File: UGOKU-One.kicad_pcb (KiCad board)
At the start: 2 copper layers, 70 x 70 mm, 57 parts, among them J2 SERVO, J3 Conn_02x03_Odd_Even, J4 14110413001000, J5 14110413001000, J6 14110413001000, P1 USB_C_Plug_USB2.0, Q2 SS8050, Q3 SS8050, SW1 PF1, SW4 SW_Push, SW5 SW_Push_DPDT, SW6 SW_Push, T4 PTS_1.5_2, T5 MultiBoardMini_Libraries:PTS_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, T6 PTS_1.5_2, U1 AMS1117-3.3, U2 CP2102N-A02-GQFN28, U3 TB67H450FNG_EL, U4 K7805M-1000R3, U5 ESP32-WROOM-32E, U8 TB67H450FNG_EL

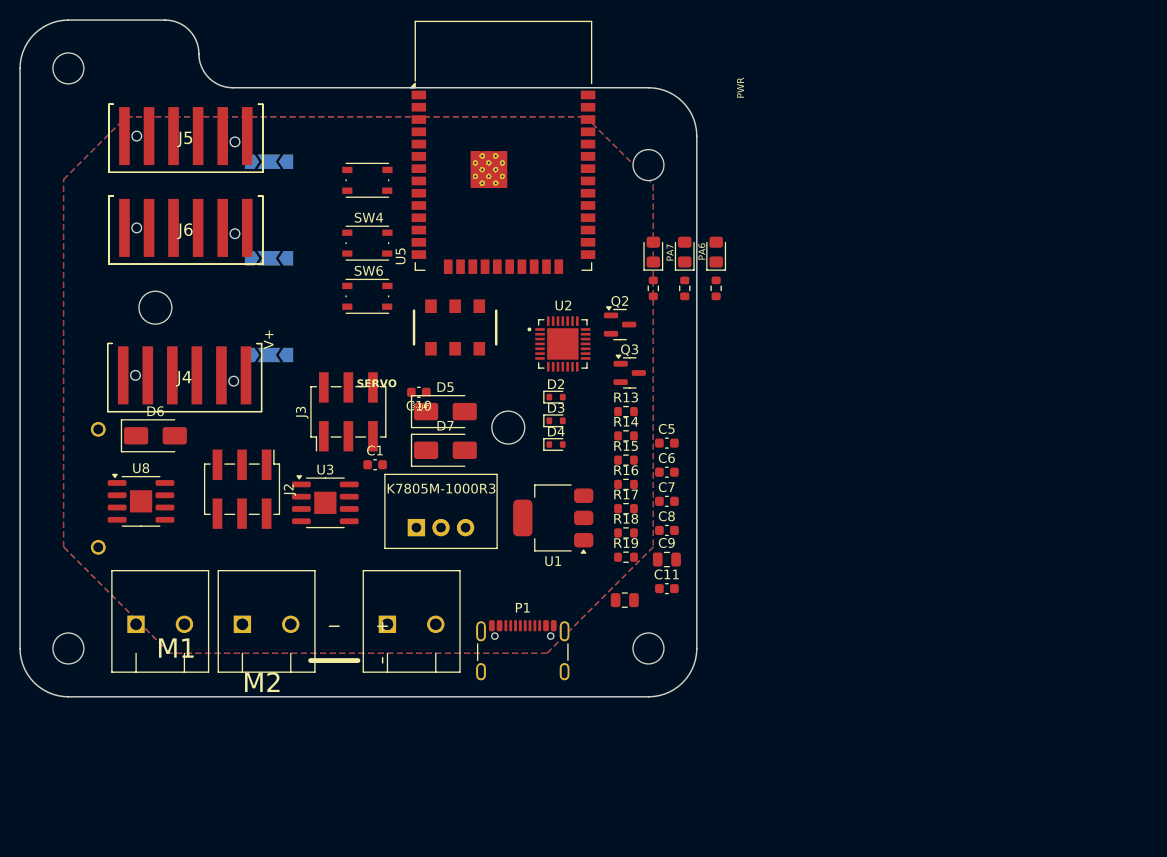
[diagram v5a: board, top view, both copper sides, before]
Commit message: Add IMU, FET
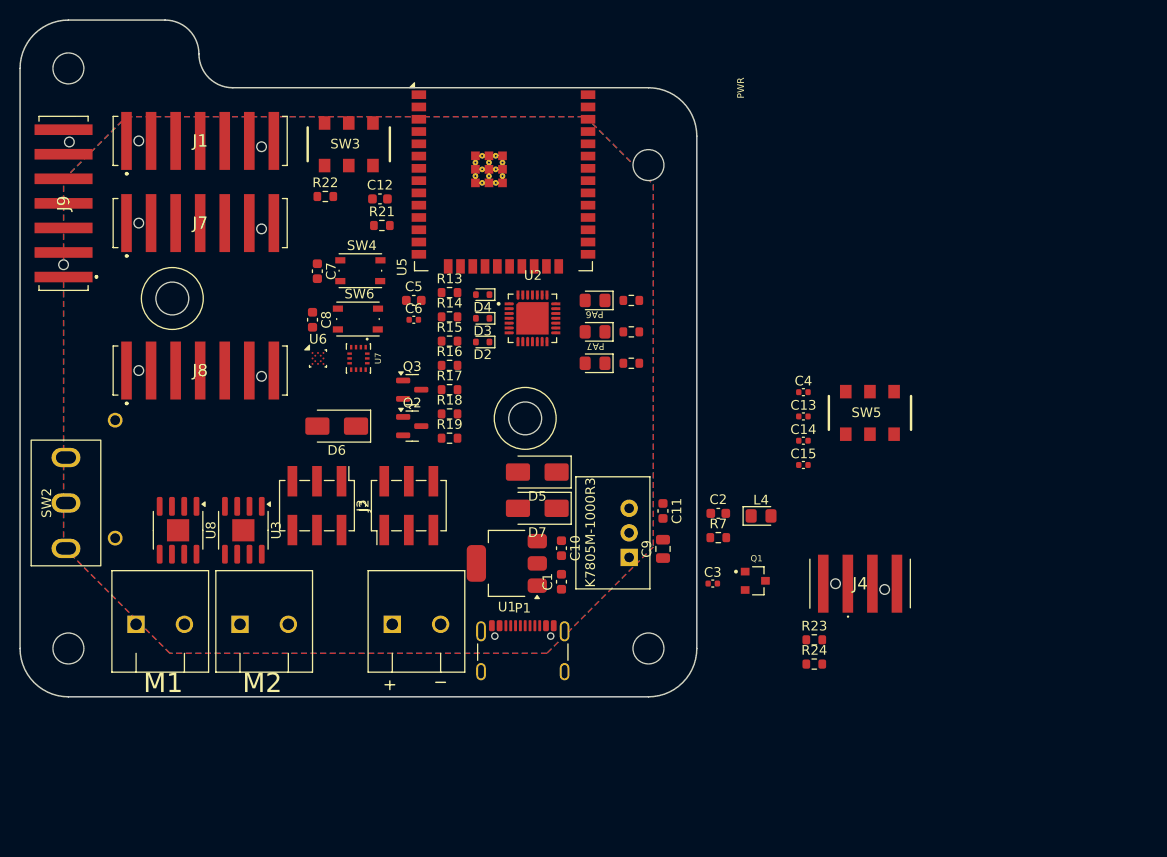
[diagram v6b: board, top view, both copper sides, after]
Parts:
- removed J5, J6: 14110413001000, 0_UGOKU-One_Lib:14110413001000
- removed JP1, JP2, JP3: Jumper_NC_Dual, Jumper:SolderJumper-3_P2.0mm_Open_TrianglePad1.0x1.5mm
- removed SW1: PF1, Button_Switch_SMD:SW_Push_1P1T_NO_Vertical_Wuerth_434133025816
- added C12: 0.1uF, Capacitor_SMD:C_0603_1608Metric, F.Cu at (2.23, -16.5)
- added C13: 0.1uF, Capacitor_SMD:C_0402_1005Metric, F.Cu at (46.0, 6.00)
- added C14: 0.1uF, Capacitor_SMD:C_0402_1005Metric, F.Cu at (46.0, 8.51)
- added C15: 0.1uF, Capacitor_SMD:C_0402_1005Metric, F.Cu at (46.0, 11.0)
- added C2: 22uF, Capacitor_SMD:C_0603_1608Metric, F.Cu at (37.2, 16.0)
- added C3: 0.1uF, Capacitor_SMD:C_0402_1005Metric, F.Cu at (36.6, 23.3)
- added J1: ENC/IO, 0_UGOKU-One_Lib:14110513001000, F.Cu at (-16.4, -22.5)
- added J7: ENC/IO, 0_UGOKU-One_Lib:14110513001000, F.Cu at (-16.4, -14.0)
- added J8: DAC, 0_UGOKU-One_Lib:14110513001000, F.Cu at (-16.4, 1.25)
- added J9: ADC, 0_UGOKU-One_Lib:14110513001000, F.Cu at (-30.5, -16.0)
- added L4: LED, LED_SMD:LED_0805_2012Metric_Pad1.15x1.40mm_HandSolder, F.Cu at (41.6, 16.3)
- added Q1: NMOS, 0_UGOKU-One_Lib:SOT-23F, F.Cu at (41.0, 23.0)
- added R21: 10k, Resistor_SMD:R_0603_1608Metric, F.Cu at (2.42, -13.8)
- added R22: 10k, Resistor_SMD:R_0603_1608Metric, F.Cu at (-3.42, -16.8)
- added R23: 10k, Resistor_SMD:R_0603_1608Metric, F.Cu at (47.1, 29.1)
- added R24: 100, Resistor_SMD:R_0603_1608Metric, F.Cu at (47.1, 31.6)
- added R7: 1k, Resistor_SMD:R_0603_1608Metric, F.Cu at (37.2, 18.5)
- added SW2: SW_SPDT, 0_UGOKU-One_Lib:SW_SS-12M11G5, F.Cu at (-30.2, 14.9)
- added SW3: SW_Slide_DPDT, 0_UGOKU-One_Lib:SSSS213202, F.Cu at (-1.00, -22.1)
- added U6: BMM150, Package_CSP:WLCSP-12_1.56x1.56mm_P0.4mm, F.Cu at (-4.18, 0.00)
- added U7: BMI270, 0_UGOKU-One_Lib:XDCR_BMI270, F.Cu at (0.00, 0.00)
- C4: value 0.1μF -> 0.1uF; footprint Capacitor_SMD:C_0805_2012Metric -> Capacitor_SMD:C_0402_1005Metric
- C6: footprint Capacitor_SMD:C_0603_1608Metric -> Capacitor_SMD:C_0402_1005Metric
- J4: value 14110413001000 -> 14110213001000; footprint 0_UGOKU-One_Lib:14110413001000 -> 0_UGOKU-One_Lib:14110213001000
- R13: value 10k -> 2K
- R14: value 10k -> 22.1k
- R15: value 10k -> 47.5k
- SW5: value SW_Push_DPDT -> SW_Slide_DPDT; footprint MultiBoardMini_Libraries:SSSS213202 -> 0_UGOKU-One_Lib:SSSS213202
- U2: footprint 0_UGOKU-One_Lib:QFN50P500X500X80-29N -> 0_UGOKU-One_Lib:IC_CP2102N-A02-GQFN28R
- U5: footprint RF_Module:ESP32-WROOM-32D -> RF_Module:ESP32-WROOM-32E
- moved J4 73.1 mm to (51.9, 23.3)
- moved SW5 43.8 mm to (52.9, 5.63)
- moved C7 43.3 mm to (-4.25, -9.03), turned to -90 degrees
- moved C8 42.6 mm to (-4.75, -4.00), turned to -90 degrees
- moved C6 30.6 mm to (5.72, -4.00)
- moved C5 30.1 mm to (5.72, -6.00)
- moved C4 28.4 mm to (46.0, 3.49), turned to 0 degrees
- moved Q2 23.9 mm to (5.56, 7.00)
- moved C1 22.8 mm to (21.0, 23.1), turned to 90 degrees
- moved Q3 22.6 mm to (5.56, 3.23)
- moved R13 22.0 mm to (9.43, -6.81)
- moved R14 22.0 mm to (9.43, -4.30)
- moved R15 22.0 mm to (9.43, -1.79)
- moved R16 22.0 mm to (9.43, 0.72)
- moved R17 22.0 mm to (9.43, 3.23)
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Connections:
- C10 pad 1: +3V3 -> 3V3
- C4 pad 1: PWR -> +3V3_IMU
- D6 pad 2: BAT_5V -> Net-(D6-A)
- J4 pad 1: Net-(J4-Pad1) -> MOT_PWR
- J4 pad 2: GND -> Net-(Q1-D)
- P1 pad A1: Net-(P1-GND-PadA1) -> GND
- P1 pad A12: Net-(P1-GND-PadA1) -> GND
- P1 pad B1: Net-(P1-GND-PadA1) -> GND
- P1 pad B12: Net-(P1-GND-PadA1) -> GND
- SW5 pad 2: Net-(SW5-B-Pad2) -> +3V3
- SW5 pad 3: GND -> +3V3_IMU
- SW5 pad 4: unconnected-(SW5-A-Pad4) -> +3V3_IMU
- SW5 pad 5: Net-(SW5-B-Pad2) -> +3V3
- SW5 pad 6: GND -> unconnected-(SW5-C-Pad6)
- U1 pad 3: +3V3 -> 3V3
- U5 pad 10: unconnected-(U5-IO25-Pad10) -> IO25
- U5 pad 11: unconnected-(U5-IO26-Pad11) -> IO26
- U5 pad 12: unconnected-(U5-IO27-Pad12) -> SERVO2
- U5 pad 14: MD2_IN1 -> unconnected-(U5-IO12-Pad14)
- U5 pad 16: MD2_IN2 -> MD1_IN2
- U5 pad 23: SERVO2 -> Slide_SW
- U5 pad 24: LED1 -> unconnected-(U5-IO2-Pad24)
- U5 pad 26: MD1_IN1 -> LED1
- U5 pad 27: unconnected-(U5-IO16-Pad27) -> LED3
- U5 pad 28: LED2 -> IO17
- U5 pad 29: MD1_IN2 -> MD1_IN1
- U5 pad 30: unconnected-(U5-IO18-Pad30) -> IO18
- U5 pad 31: unconnected-(U5-IO19-Pad31) -> IO19
- U5 pad 33: unconnected-(U5-IO21-Pad33) -> SDA
- U5 pad 36: unconnected-(U5-IO22-Pad36) -> SCL
- U5 pad 37: unconnected-(U5-IO23-Pad37) -> LED2
- U5 pad 4: unconnected-(U5-SENSOR_VP-Pad4) -> SENS_VP
- U5 pad 5: unconnected-(U5-SENSOR_VN-Pad5) -> SENS_VN
- U5 pad 6: unconnected-(U5-IO34-Pad6) -> IO34
- U5 pad 7: unconnected-(U5-IO35-Pad7) -> IO35
- U5 pad 8: unconnected-(U5-IO32-Pad8) -> MD2_IN1
- U5 pad 9: unconnected-(U5-IO33-Pad9) -> MD2_IN2
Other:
- board text removed: "3.3μF"
- board text removed: "3V3 5V"
- board text removed: "SERVO"
- board text removed: "V+"

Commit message: power layout draft
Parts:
- added C16: 10μF, Capacitor_SMD:C_0805_2012Metric, F.Cu at (-15.7, 19.8)
- added C17: 0.1μF, Capacitor_SMD:C_0402_1005Metric, F.Cu at (-13.9, 19.3)
- added C18: 0.1μF, Capacitor_SMD:C_0402_1005Metric, F.Cu at (-22.5, 19.7)
- added C19: 10μF, Capacitor_SMD:C_0805_2012Metric, F.Cu at (-23.7, 19.9)
- added D8: SS54, Diode_SMD:D_SMA, F.Cu at (15.0, 1.50)
- C12, C7, C8: footprint Capacitor_SMD:C_0603_1608Metric -> Capacitor_SMD:C_0402_1005Metric
- J4: footprint 0_UGOKU-One_Lib:14110213001000 -> 0_UGOKU-One_Lib:14010213102000
- R13, R14, R15, R16, R17, R18, R19, R21, R22, R23, R24: footprint Resistor_SMD:R_0603_1608Metric -> Resistor_SMD:R_0402_1005Metric
- moved C13 50.9 mm to (-4.25, -1.75)
- moved C4 50.3 mm to (-4.25, 1.75), turned to 180 degrees
- moved C15 49.3 mm to (-2.00, 0.00), turned to 90 degrees
- moved SW5 46.4 mm to (6.50, 4.30)
- moved C14 44.8 mm to (2.00, 0.00), turned to 90 degrees
- moved L4 35.4 mm to (13.8, -5.50), turned to 90 degrees
- moved C3 31.6 mm to (17.8, -2.08), turned to 90 degrees
- moved R24 31.3 mm to (22.0, 13.0), turned to 90 degrees
- moved R7 31.2 mm to (13.5, -1.75), turned to 90 degrees
- moved R23 31.1 mm to (20.5, 13.0), turned to 90 degrees
- moved J4 28.6 mm to (27.7, 8.00), turned to -90 degrees
- moved C2 27.7 mm to (16.2, -2.10), turned to 90 degrees
- moved Q3 27.2 mm to (27.8, -12.5), turned to 180 degrees
- moved Q2 26.4 mm to (28.2, -6.50)
- moved R4 24.0 mm to (4.35, -1.69), turned to 90 degrees
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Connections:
- net +3V3_IMU renamed 3V3_IMU
- net Net-(U3-OUT1) renamed /MD1_OUT1
- net Net-(U3-OUT2) renamed /MD1_OUT2
- net Net-(U8-OUT1) renamed /MD2_OUT1
- net Net-(U8-OUT2) renamed /MD2_OUT2
- C2 pad 1: +3V3 -> 3V3
- C3 pad 1: +3V3 -> 3V3
- C5 pad 1: +3V3 -> 3V3
- C6 pad 1: +3V3 -> 3V3
- L1 pad 2: +3V3 -> 3V3
- R13 pad 2: +3V3 -> 3V3
- R21 pad 1: +3V3 -> 3V3
- R22 pad 1: +3V3 -> 3V3
- SW5 pad 2: +3V3 -> 3V3
- SW5 pad 5: +3V3 -> 3V3
- U2 pad 6: +3V3 -> 3V3
- U2 pad 7: +3V3 -> 3V3
- U3 pad 4: +5V -> 5V
- U5 pad 2: +3V3 -> 3V3
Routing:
- net GND: track 0.00 -> 122.1 mm
- net 5V: track 0.00 -> 107.2 mm, vias 0 -> 3
- net MOT_PWR: track 0.00 -> 94.9 mm
- net PWR: track 0.00 -> 32.9 mm
- net Net-(D6-A): track 0.00 -> 27.9 mm, vias 0 -> 1
- net SERVO_PWR: track 0.00 -> 19.4 mm
- net Net-(D7-A): track 0.00 -> 16.4 mm
- net Net-(D8-A): track 0.00 -> 8.29 mm
- net /MD1_OUT2: track 0.00 -> 7.41 mm
- net /MD1_OUT1: track 0.00 -> 6.97 mm
- net 3V3: track 0.00 -> 2.52 mm
- net BAT_5V: track 0.00 -> 1.45 mm
- net USB_5V: track 0.00 -> 0.60 mm
- added copper zone on F.Cu, net /MD2_OUT1

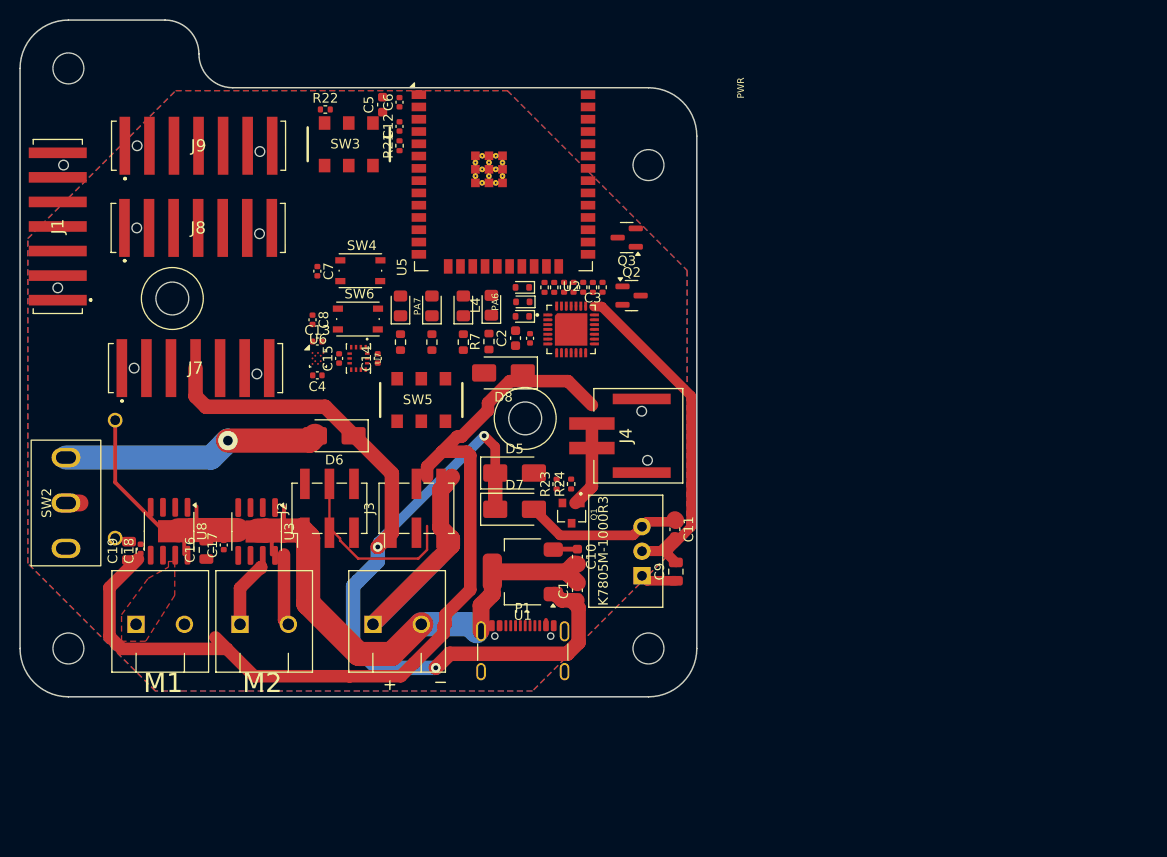
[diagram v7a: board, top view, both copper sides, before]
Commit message: Power:near complete
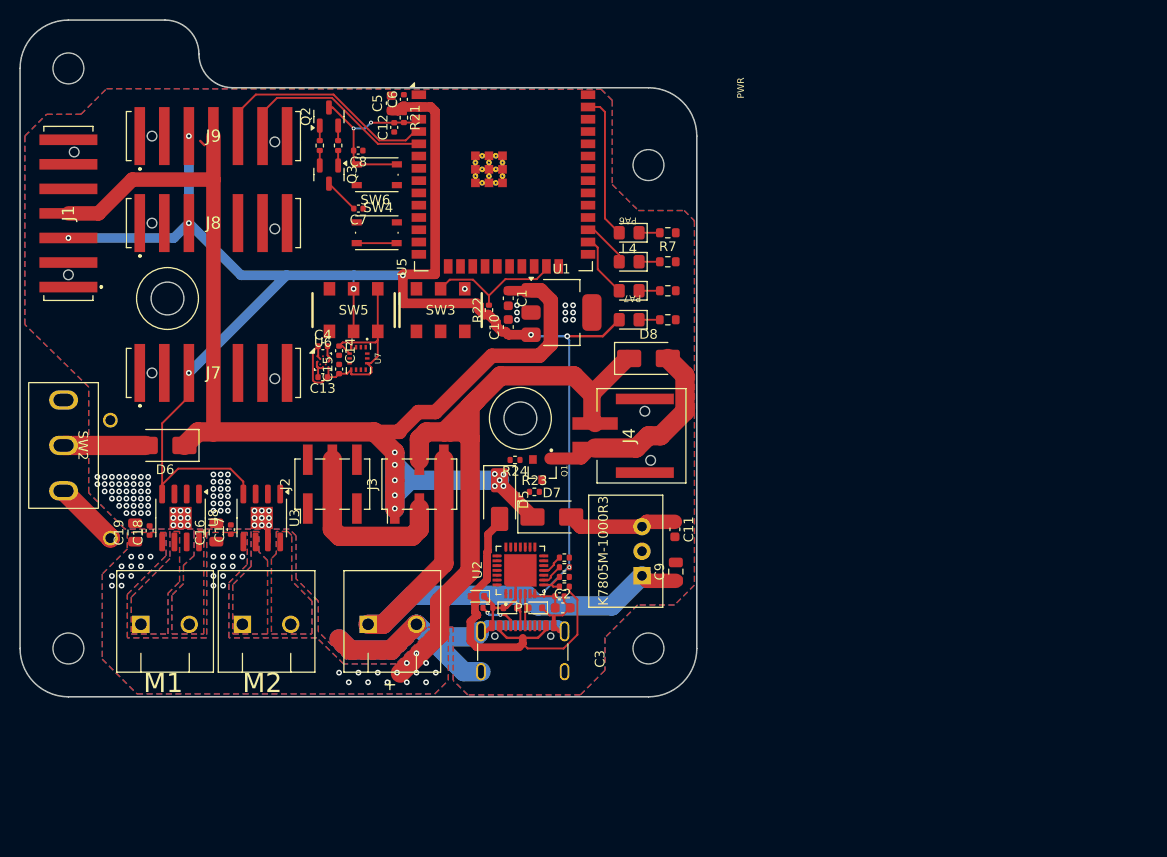
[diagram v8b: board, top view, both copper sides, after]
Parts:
- moved Q2 36.4 mm to (-3.05, -25.0), turned to 90 degrees
- moved R17 34.1 mm to (13.4, 25.8), turned to 180 degrees
- moved D2 32.3 mm to (12.3, 24.6)
- moved D3 31.7 mm to (18.3, 25.8)
- moved Q3 31.5 mm to (-3.05, -19.0), turned to -90 degrees
- moved R14 31.1 mm to (21.3, 23.6), turned to 0 degrees
- moved C1 31.0 mm to (15.5, -6.22), turned to -90 degrees
- moved D4 30.2 mm to (15.7, 25.8), turned to 0 degrees
- moved R15 30.0 mm to (21.3, 22.6), turned to 180 degrees
- moved R13 29.2 mm to (21.3, 21.6), turned to 0 degrees
- moved R18 28.3 mm to (-4.00, -22.0)
- moved C2 28.3 mm to (21.1, 25.8), turned to 0 degrees
- moved R16 28.0 mm to (21.3, 20.6), turned to 180 degrees
- moved R4 27.7 mm to (32.0, -4.00), turned to 180 degrees
- moved U1 27.1 mm to (21.0, -4.75), turned to 0 degrees
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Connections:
- J9 pad 4: SENS_VN -> SENS_VP
- J9 pad 5: SENS_VP -> SENS_VN
- SW2 pad 2: BAT_5V -> Net-(D6-A)
- SW2 pad 3: Net-(D6-A) -> BAT_5V
- SW3 pad 4: GND -> unconnected-(SW3-C-Pad4)
- SW3 pad 6: unconnected-(SW3-C-Pad6) -> GND
- SW5 pad 4: 3V3_IMU -> unconnected-(SW5-C-Pad4)
- SW5 pad 6: unconnected-(SW5-C-Pad6) -> 3V3_IMU
- U3 pad 4: 5V -> 3V3
- U5 pad 27: LED3 -> LED2
- U5 pad 37: LED2 -> LED3
- U8 pad 4: +5V -> 3V3
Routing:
- net 3V3: track 2.52 -> 177.3 mm, vias 0 -> 10
- net GND: track 122.1 -> 69.3 mm, vias 0 -> 84
- net USB_5V: track 0.60 -> 39.1 mm
- net 3V3_IMU: track 0.00 -> 28.7 mm
- net MOT_PWR: track 94.9 -> 66.4 mm, vias 0 -> 36
- net 5V: track 107.2 -> 135.1 mm, vias 3 -> 10
- net SENS_VP: track 0.00 -> 24.3 mm
- net PWR: track 32.9 -> 56.2 mm
- net SENS_VN: track 0.00 -> 21.2 mm
- net Net-(D6-A): track 27.9 -> 8.50 mm, vias 1 -> 0
- net EN: track 0.00 -> 18.6 mm, vias 0 -> 2
- net LED3: track 0.00 -> 15.1 mm
- net Slide_SW: track 0.00 -> 14.4 mm
- net Net-(D8-A): track 8.29 -> 21.8 mm
- net IO0: track 0.00 -> 7.77 mm
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- added copper zone on B.Cu, net /MD1_OUT1
- added copper zone on F.Cu, net /MD1_OUT1
- added copper zone on B.Cu, net /MD1_OUT2
- added copper zone on F.Cu, net /MD1_OUT2
- added copper zone on B.Cu, net /MD2_OUT1
- added copper zone on B.Cu, net /MD2_OUT2
- added copper zone on F.Cu, net /MD2_OUT2
- added copper zone on B.Cu, net MOT_PWR
- added copper zone on F.Cu, net MOT_PWR
